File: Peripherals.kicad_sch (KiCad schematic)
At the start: 10 parts, among them J2 Micro_SD_Card_Det1, U2 MS5611 #1, U3 MS5611 #2, U4 LIS3DH, U5 H3LIS331DL

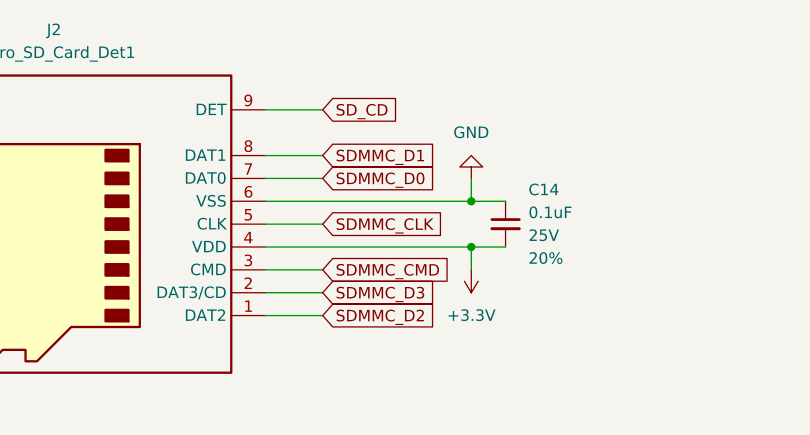
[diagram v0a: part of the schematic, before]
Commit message: feat: finish schematic (erc_pass)
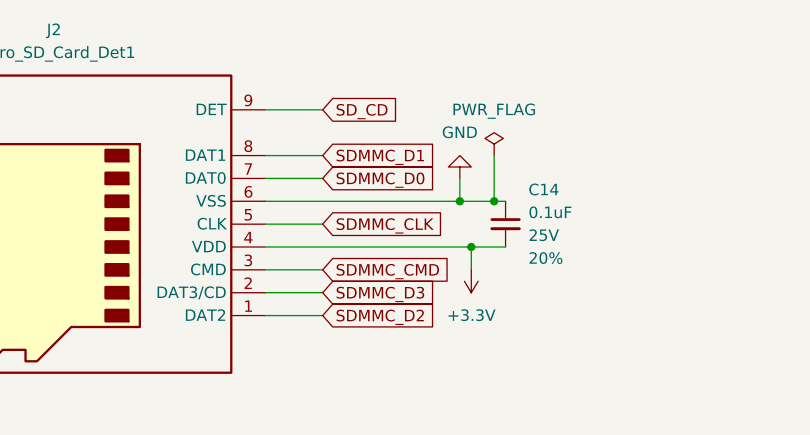
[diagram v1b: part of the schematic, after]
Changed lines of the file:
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@@
 	)
 	(junction
-		(at 110.49 48.26)
+		(at 109.22 48.26)
 		(diameter 0)
 		(color 0 0 0 0)
 	)
+	(junction
+		(at 113.03 48.26)
+		(diameter 0)
+		(color 0 0 0 0)
+	)
 	(no_connect
 		(at 251.46 72.39)
@@
 	(wire
 		(pts
-			(xy 110.49 48.26) (xy 114.3 48.26)
+			(xy 87.63 48.26) (xy 109.22 48.26)
 		)
 		(stroke
@@
 	(wire
 		(pts
+			(xy 109.22 48.26) (xy 113.03 48.26)
+		)
+		(stroke
+			(width 0)
+			(type default)
+		)
+	)
+	(wire
+		(pts
 			(xy 241.3 57.15) (xy 241.3 54.61)
 		)
@@
 	(wire
 		(pts
-			(xy 87.63 48.26) (xy 110.49 48.26)
+			(xy 109.22 45.72) (xy 109.22 48.26)
 		)
 		(stroke
@@
 	(wire
 		(pts
-			(xy 110.49 45.72) (xy 110.49 48.26)
-		)
-		(stroke
-			(width 0)
-			(type default)
-		)
-	)
-	(wire
-		(pts
 			(xy 87.63 60.96) (xy 93.98 60.96)
 		)
@@
 		(pts
 			(xy 87.63 38.1) (xy 93.98 38.1)
+		)
+		(stroke
+			(width 0)
+			(type default)
+		)
+	)
+	(wire
+		(pts
+			(xy 113.03 43.18) (xy 113.03 48.26)
+		)
+		(stroke
+			(width 0)
+			(type default)
+		)
+	)
+	(wire
+		(pts
+			(xy 113.03 48.26) (xy 114.3 48.26)
 		)
 		(stroke
@@
 	(symbol
 		(lib_id "power:GND")
-		(at 110.49 45.72 180)
-		(unit 1)
-		(body_style 1)
-		(exclude_from_sim no)
-		(in_bom yes)
-		(on_board yes)
-		(in_pos_files yes)
-		(dnp no)
-		(fields_autoplaced yes)
-		(property "Reference" "#PWR023"
-			(at 110.49 39.37 0)
-			(hide yes)
-			(show_name no)
-			(do_not_autoplace no)
-			(effects
-				(font
-					(size 1.27 1.27)
-				)
-			)
-		)
-		(property "Value" "GND"
-			(at 110.49 40.64 0)
-			(show_name no)
-			(do_not_autoplace no)
-			(effects
-				(font
-					(size 1.27 1.27)
-				)
-			)
-		)
-		(property "Footprint" ""
-			(at 110.49 45.72 0)
-			(hide yes)
-			(show_name no)
-			(do_not_autoplace no)
-			(effects
-				(font
-					(size 1.27 1.27)
-				)
-			)
-		)
-		(property "Datasheet" ""
-			(at 110.49 45.72 0)
-			(hide yes)
-			(show_name no)
-			(do_not_autoplace no)
-			(effects
-				(font
-					(size 1.27 1.27)
-				)
-			)
-		)
-		(property "Description" "Power symbol creates a global label with name \"GND\" , ground"
-			(at 110.49 45.72 0)
-			(hide yes)
-			(show_name no)
-			(do_not_autoplace no)
-			(effects
-				(font
-					(size 1.27 1.27)
-				)
-			)
-		)
-		(pin "1"
-		)
-		(instances
-			(project "UNSW_Rocketry_Senior_Flight_Computer"
-				(path "/9e0253f5-fba5-4205-8256-7fc47a91dd1e/e7df30d3-5847-4b99-8916-a8021a668802"
-					(reference "#PWR023")
-					(unit 1)
-				)
-			)
-		)
-	)
-	(symbol
-		(lib_id "power:GND")
 		(at 191.77 116.84 90)
 		(unit 1)
@@
 				(path "/9e0253f5-fba5-4205-8256-7fc47a91dd1e/e7df30d3-5847-4b99-8916-a8021a668802"
 					(reference "C14")
+					(unit 1)
+				)
+			)
+		)
+	)
+	(symbol
+		(lib_id "power:GND")
+		(at 109.22 45.72 180)
+		(unit 1)
+		(body_style 1)
+		(exclude_from_sim no)
+		(in_bom yes)
+		(on_board yes)
+		(in_pos_files yes)
+		(dnp no)
+		(fields_autoplaced yes)
+		(property "Reference" "#PWR023"
+			(at 109.22 39.37 0)
+			(hide yes)
+			(show_name no)
+			(do_not_autoplace no)
+			(effects
+				(font
+					(size 1.27 1.27)
+				)
+			)
+		)
+		(property "Value" "GND"
+			(at 109.22 40.64 0)
+			(show_name no)
+			(do_not_autoplace no)
+			(effects
+				(font
+					(size 1.27 1.27)
+				)
+			)
+		)
+		(property "Footprint" ""
+			(at 109.22 45.72 0)
+			(hide yes)
+			(show_name no)
+			(do_not_autoplace no)
+			(effects
+				(font
+					(size 1.27 1.27)
+				)
+			)
+		)
+		(property "Datasheet" ""
+			(at 109.22 45.72 0)
+			(hide yes)
+			(show_name no)
+			(do_not_autoplace no)
+			(effects
+				(font
+					(size 1.27 1.27)
+				)
+			)
+		)
+		(property "Description" "Power symbol creates a global label with name \"GND\" , ground"
+			(at 109.22 45.72 0)
+			(hide yes)
+			(show_name no)
+			(do_not_autoplace no)
+			(effects
+				(font
+					(size 1.27 1.27)
+				)
+			)
+		)
+		(pin "1"
+		)
+		(instances
+			(project "UNSW_Rocketry_Senior_Flight_Computer"
+				(path "/9e0253f5-fba5-4205-8256-7fc47a91dd1e/e7df30d3-5847-4b99-8916-a8021a668802"
+					(reference "#PWR023")
 					(unit 1)
 				)
@@
 					(unit 1)
 				)
+			)
+		)
+	)
+	(symbol
+		(lib_id "power:PWR_FLAG")
+		(at 113.03 43.18 0)
+		(unit 1)
+		(body_style 1)
+		(exclude_from_sim no)
+		(in_bom yes)
+		(on_board yes)
+		(in_pos_files yes)
+		(dnp no)
+		(fields_autoplaced yes)
+		(property "Reference" "#FLG03"
+			(at 113.03 41.275 0)
+			(hide yes)
+			(show_name no)
+			(do_not_autoplace no)
+			(effects
+				(font
+					(size 1.27 1.27)
+				)
+			)
+		)
+		(property "Value" "PWR_FLAG"
+			(at 113.03 38.1 0)
+			(show_name no)
+			(do_not_autoplace no)
+			(effects
+				(font
+					(size 1.27 1.27)
+				)
+			)
+		)
+		(property "Footprint" ""
+			(at 113.03 43.18 0)
+			(hide yes)
+			(show_name no)
+			(do_not_autoplace no)
+			(effects
+				(font
+					(size 1.27 1.27)
+				)
+			)
+		)
+		(property "Datasheet" ""
+			(at 113.03 43.18 0)
+			(hide yes)
+			(show_name no)
+			(do_not_autoplace no)
+			(effects
+				(font
+					(size 1.27 1.27)
+				)
+			)
+		)
+		(property "Description" "Special symbol for telling ERC where power comes from"
+			(at 113.03 43.18 0)
+			(hide yes)
+			(show_name no)
+			(do_not_autoplace no)
+			(effects
+				(font
+					(size 1.27 1.27)
+				)
+			)
+		)
+		(pin "1"
+		)
+		(instances
+			(project "UNSW_Rocketry_Senior_Flight_Computer"
+				(path "/9e0253f5-fba5-4205-8256-7fc47a91dd1e/e7df30d3-5847-4b99-8916-a8021a668802"
+					(reference "#FLG03")
+					(unit 1)
+				)

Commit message: feat: finish schematic (Full)
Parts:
- J2: footprint (none) -> Connector_Card:microSD_HC_Hirose_DM3AT-SF-PEJM5
- renumbered C14 to C24, C16 to C25, C20 to C26, C21 to C27, C19 to C28, U5 to U4, U2 to U5, U4 to U6, U3 to U7
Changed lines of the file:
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@@
 		(dnp no)
 		(fields_autoplaced yes)
-		(property "Reference" "#PWR031"
+		(property "Reference" "#PWR054"
 			(at 209.55 81.28 0)
 			(hide yes)
@@
 			(project "UNSW_Rocketry_Senior_Flight_Computer"
 				(path "/9e0253f5-fba5-4205-8256-7fc47a91dd1e/e7df30d3-5847-4b99-8916-a8021a668802"
-					(reference "#PWR031")
+					(reference "#PWR054")
 					(unit 1)
 				)
@@
 		(dnp no)
 		(fields_autoplaced yes)
-		(property "Reference" "#PWR048"
+		(property "Reference" "#PWR049"
 			(at 162.56 54.61 0)
 			(hide yes)
@@
 			(project "UNSW_Rocketry_Senior_Flight_Computer"
 				(path "/9e0253f5-fba5-4205-8256-7fc47a91dd1e/e7df30d3-5847-4b99-8916-a8021a668802"
-					(reference "#PWR048")
+					(reference "#PWR049")
 					(unit 1)
 				)
@@
 		(dnp no)
 		(fields_autoplaced yes)
-		(property "Reference" "#PWR047"
+		(property "Reference" "#PWR053"
 			(at 198.12 116.84 0)
 			(hide yes)
@@
 			(project "UNSW_Rocketry_Senior_Flight_Computer"
 				(path "/9e0253f5-fba5-4205-8256-7fc47a91dd1e/e7df30d3-5847-4b99-8916-a8021a668802"
-					(reference "#PWR047")
+					(reference "#PWR053")
 					(unit 1)
 				)
@@
 		(dnp no)
 		(fields_autoplaced yes)
-		(property "Reference" "#PWR042"
+		(property "Reference" "#PWR055"
 			(at 222.25 116.84 0)
 			(hide yes)
@@
 			(project "UNSW_Rocketry_Senior_Flight_Computer"
 				(path "/9e0253f5-fba5-4205-8256-7fc47a91dd1e/e7df30d3-5847-4b99-8916-a8021a668802"
-					(reference "#PWR042")
+					(reference "#PWR055")
 					(unit 1)
 				)
@@
 		(dnp no)
 		(fields_autoplaced yes)
-		(property "Reference" "C14"
+		(property "Reference" "C24"
 			(at 116.84 46.9962 0)
 			(show_name no)
@@
 			(project "UNSW_Rocketry_Senior_Flight_Computer"
 				(path "/9e0253f5-fba5-4205-8256-7fc47a91dd1e/e7df30d3-5847-4b99-8916-a8021a668802"
-					(reference "C14")
+					(reference "C24")
 					(unit 1)
 				)
@@
 		(dnp no)
 		(fields_autoplaced yes)
-		(property "Reference" "#PWR023"
+		(property "Reference" "#PWR047"
 			(at 109.22 39.37 0)
 			(hide yes)
@@
 			(project "UNSW_Rocketry_Senior_Flight_Computer"
 				(path "/9e0253f5-fba5-4205-8256-7fc47a91dd1e/e7df30d3-5847-4b99-8916-a8021a668802"
-					(reference "#PWR023")
+					(reference "#PWR047")
 					(unit 1)
 				)
@@
 		(in_pos_files yes)
 		(dnp no)
-		(property "Reference" "U5"
+		(property "Reference" "U4"
 			(at 174.244 83.82 0)
 			(show_name no)
@@
 			(project "UNSW_Rocketry_Senior_Flight_Computer"
 				(path "/9e0253f5-fba5-4205-8256-7fc47a91dd1e/e7df30d3-5847-4b99-8916-a8021a668802"
-					(reference "U5")
+					(reference "U4")
 					(unit 1)
 				)
@@
 		(dnp no)
 		(fields_autoplaced yes)
-		(property "Reference" "#PWR050"
+		(property "Reference" "#PWR058"
 			(at 238.76 116.84 0)
 			(hide yes)
@@
 			(project "UNSW_Rocketry_Senior_Flight_Computer"
 				(path "/9e0253f5-fba5-4205-8256-7fc47a91dd1e/e7df30d3-5847-4b99-8916-a8021a668802"
-					(reference "#PWR050")
+					(reference "#PWR058")
 					(unit 1)
 				)
@@
 		(dnp no)
 		(fields_autoplaced yes)
-		(property "Reference" "#PWR052"
+		(property "Reference" "#PWR051"
 			(at 179.07 57.15 0)
 			(hide yes)
@@
 			(project "UNSW_Rocketry_Senior_Flight_Computer"
 				(path "/9e0253f5-fba5-4205-8256-7fc47a91dd1e/e7df30d3-5847-4b99-8916-a8021a668802"
-					(reference "#PWR052")
+					(reference "#PWR051")
 					(unit 1)
 				)
@@
 		(dnp no)
 		(fields_autoplaced yes)
-		(property "Reference" "#PWR053"
+		(property "Reference" "#PWR057"
 			(at 241.3 57.15 0)
 			(hide yes)
@@
 			(project "UNSW_Rocketry_Senior_Flight_Computer"
 				(path "/9e0253f5-fba5-4205-8256-7fc47a91dd1e/e7df30d3-5847-4b99-8916-a8021a668802"
-					(reference "#PWR053")
+					(reference "#PWR057")
 					(unit 1)
 				)
@@
 		(in_pos_files yes)
 		(dnp no)
-		(property "Reference" "C20"
+		(property "Reference" "C26"
 			(at 186.69 120.65 90)
 			(show_name no)
@@
 			(project "UNSW_Rocketry_Senior_Flight_Computer"
 				(path "/9e0253f5-fba5-4205-8256-7fc47a91dd1e/e7df30d3-5847-4b99-8916-a8021a668802"
-					(reference "C20")
+					(reference "C26")
 					(unit 1)
 				)
@@
 		(dnp no)
 		(fields_autoplaced yes)
-		(property "Reference" "#PWR054"
+		(property "Reference" "#PWR056"
 			(at 237.49 53.34 0)
 			(hide yes)
@@
 			(project "UNSW_Rocketry_Senior_Flight_Computer"
 				(path "/9e0253f5-fba5-4205-8256-7fc47a91dd1e/e7df30d3-5847-4b99-8916-a8021a668802"
-					(reference "#PWR054")
+					(reference "#PWR056")
 					(unit 1)
 				)
@@
 		(dnp no)
 		(fields_autoplaced yes)
-		(property "Reference" "#PWR051"
+		(property "Reference" "#PWR050"
 			(at 181.61 116.84 0)
 			(hide yes)
@@
 			(project "UNSW_Rocketry_Senior_Flight_Computer"
 				(path "/9e0253f5-fba5-4205-8256-7fc47a91dd1e/e7df30d3-5847-4b99-8916-a8021a668802"
-					(reference "#PWR051")
+					(reference "#PWR050")
 					(unit 1)
 				)
@@
 			)
 		)
-		(property "Footprint" ""
+		(property "Footprint" "Connector_Card:microSD_HC_Hirose_DM3AT-SF-PEJM5"
 			(at 12.7 68.58 0)
 			(hide yes)
@@
 		(dnp no)
 		(fields_autoplaced yes)
-		(property "Reference" "#PWR024"
+		(property "Reference" "#PWR048"
 			(at 110.49 52.07 0)
 			(hide yes)
@@
 			(project "UNSW_Rocketry_Senior_Flight_Computer"
 				(path "/9e0253f5-fba5-4205-8256-7fc47a91dd1e/e7df30d3-5847-4b99-8916-a8021a668802"
-					(reference "#PWR024")
+					(reference "#PWR048")
 					(unit 1)
 				)
@@
 		(dnp no)
 		(fields_autoplaced yes)
-		(property "Reference" "#FLG03"
+		(property "Reference" "#FLG02"
 			(at 113.03 41.275 0)
 			(hide yes)
@@
 			(project "UNSW_Rocketry_Senior_Flight_Computer"
 				(path "/9e0253f5-fba5-4205-8256-7fc47a91dd1e/e7df30d3-5847-4b99-8916-a8021a668802"
-					(reference "#FLG03")
+					(reference "#FLG02")
 					(unit 1)
 				)
@@
 		(dnp no)
 		(fields_autoplaced yes)
-		(property "Reference" "C16"
+		(property "Reference" "C25"
 			(at 173.9836 43.18 90)
 			(show_name no)
@@
 			(project "UNSW_Rocketry_Senior_Flight_Computer"
 				(path "/9e0253f5-fba5-4205-8256-7fc47a91dd1e/e7df30d3-5847-4b99-8916-a8021a668802"
-					(reference "C16")
+					(reference "C25")
 					(unit 1)
 				)
@@
 		(dnp no)
 		(fields_autoplaced yes)
-		(property "Reference" "#PWR025"
+		(property "Reference" "#PWR046"
 			(at 33.02 38.1 0)
 			(hide yes)
@@
 			(project "UNSW_Rocketry_Senior_Flight_Computer"
 				(path "/9e0253f5-fba5-4205-8256-7fc47a91dd1e/e7df30d3-5847-4b99-8916-a8021a668802"
-					(reference "#PWR025")
+					(reference "#PWR046")
 					(unit 1)
 				)
@@
 		(dnp no)
 		(fields_autoplaced yes)
-		(property "Reference" "#PWR055"
+		(property "Reference" "#PWR052"
 			(at 182.88 54.61 0)
 			(hide yes)
@@
 			(project "UNSW_Rocketry_Senior_Flight_Computer"
 				(path "/9e0253f5-fba5-4205-8256-7fc47a91dd1e/e7df30d3-5847-4b99-8916-a8021a668802"
-					(reference "#PWR055")
+					(reference "#PWR052")
 					(unit 1)
 				)
@@
 		(dnp no)
 		(fields_autoplaced yes)
-		(property "Reference" "#PWR041"
+		(property "Reference" "#PWR059"
 			(at 257.81 54.61 0)
 			(hide yes)
@@
 			(project "UNSW_Rocketry_Senior_Flight_Computer"
 				(path "/9e0253f5-fba5-4205-8256-7fc47a91dd1e/e7df30d3-5847-4b99-8916-a8021a668802"
-					(reference "#PWR041")
+					(reference "#PWR059")
 					(unit 1)
 				)
@@
 		(in_pos_files yes)
 		(dnp no)
-		(property "Reference" "U2"
+		(property "Reference" "U5"
 			(at 172.72 105.4101 0)
 			(show_name no)
@@
 			(project "UNSW_Rocketry_Senior_Flight_Computer"
 				(path "/9e0253f5-fba5-4205-8256-7fc47a91dd1e/e7df30d3-5847-4b99-8916-a8021a668802"
-					(reference "U2")
+					(reference "U5")
 					(unit 1)
 				)
@@
 		(dnp no)
 		(fields_autoplaced yes)
-		(property "Reference" "C19"
+		(property "Reference" "C28"
 			(at 246.3736 43.18 90)
 			(show_name no)
@@
 			(project "UNSW_Rocketry_Senior_Flight_Computer"
 				(path "/9e0253f5-fba5-4205-8256-7fc47a91dd1e/e7df30d3-5847-4b99-8916-a8021a668802"
-					(reference "C19")
+					(reference "C28")
 					(unit 1)
 				)
@@
 		(in_pos_files yes)
 		(dnp no)
-		(property "Reference" "C21"
+		(property "Reference" "C27"
 			(at 233.68 120.65 90)
 			(show_name no)
@@
 			(project "UNSW_Rocketry_Senior_Flight_Computer"
 				(path "/9e0253f5-fba5-4205-8256-7fc47a91dd1e/e7df30d3-5847-4b99-8916-a8021a668802"
-					(reference "C21")
+					(reference "C27")
 					(unit 1)
 				)
@@
 		(in_pos_files yes)
 		(dnp no)
-		(property "Reference" "U4"
+		(property "Reference" "U6"
 			(at 242.062 84.074 0)
 			(show_name no)
@@
 			(project "UNSW_Rocketry_Senior_Flight_Computer"
 				(path "/9e0253f5-fba5-4205-8256-7fc47a91dd1e/e7df30d3-5847-4b99-8916-a8021a668802"
-					(reference "U4")
+					(reference "U6")
 					(unit 1)
 				)
@@
 		(dnp no)
 		(fields_autoplaced yes)
-		(property "Reference" "U3"
+		(property "Reference" "U7"
 			(at 247.65 105.4101 0)
 			(show_name no)
@@
 			(project "UNSW_Rocketry_Senior_Flight_Computer"
 				(path "/9e0253f5-fba5-4205-8256-7fc47a91dd1e/e7df30d3-5847-4b99-8916-a8021a668802"
-					(reference "U3")
-					(unit 1)
-				)
+					(reference "U7")
+					(unit 1)
+				)
